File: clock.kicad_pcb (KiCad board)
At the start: 2 copper layers, 129 parts, among them J1 USB_C_Receptacle_USB2.0_16P, J3 Conn_01x02_Pin, J4 Conn_01x02_Pin, Q1 2N7002K, Q2 NPN, U1 STM32F072CBT6, U2 USBLC6-2SC6, U4 MCP73871-2CC, U5 AP2112K-3.3, Y1 8MHz

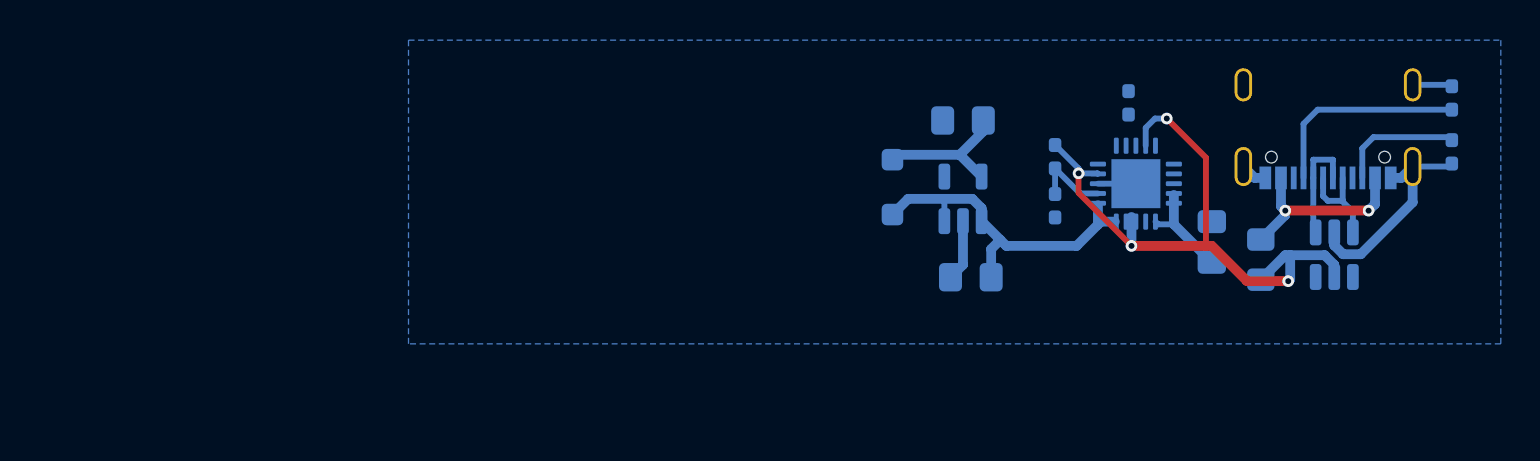
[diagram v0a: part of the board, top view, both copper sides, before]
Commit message: rerouting to flip the usb to the other side
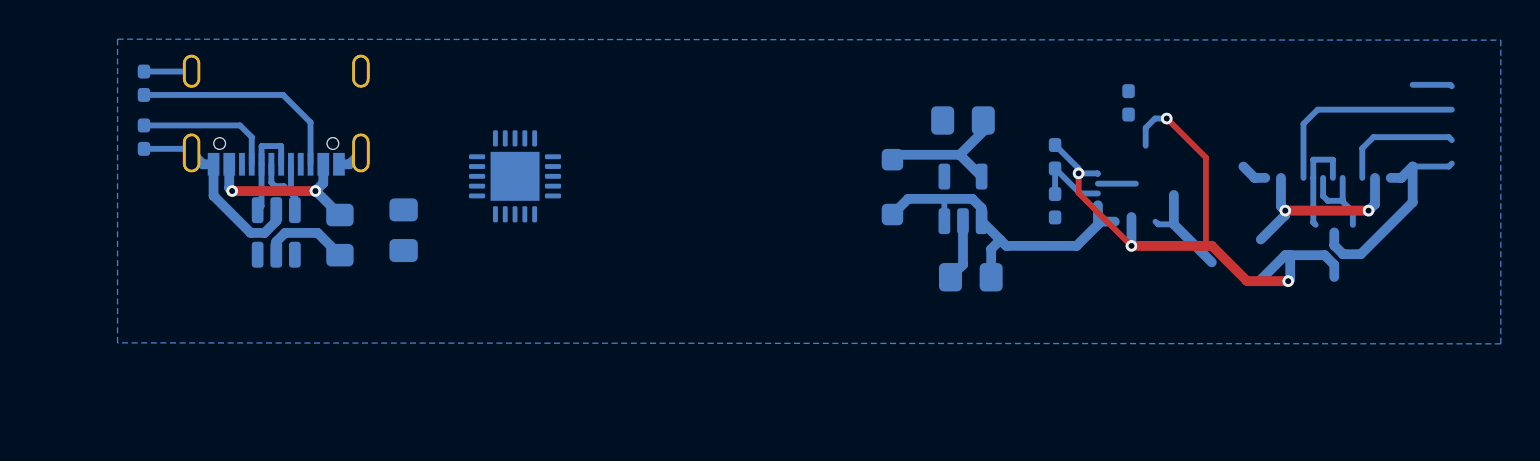
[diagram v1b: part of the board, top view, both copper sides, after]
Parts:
- moved R1 66.8 mm to (206.0, 28.5), turned to -90 degrees
- moved R2 66.8 mm to (206.0, 31.2), turned to 90 degrees
- moved U2 54.0 mm to (212.8, 36.1)
- moved J1 53.7 mm to (212.8, 30.1)
- moved F1 47.0 mm to (216.0, 36.2)
- moved C17 41.3 mm to (219.2, 36.0)
- moved U4 31.7 mm to (224.9, 33.2), turned to 180 degrees
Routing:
- net GND: track 19.7 -> 33.7 mm
- net Net-(J1-CC2): track 6.38 -> 17.6 mm
- net /VBUS: track 9.81 -> 18.8 mm, vias 2 -> 4
- net Net-(J1-CC1): track 10.6 -> 17.8 mm
- net D_BUS-: track 5.30 -> 10.6 mm
- net D_BUS+: track 4.63 -> 9.49 mm
- net +5V: track 34.1 -> 38.7 mm

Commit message: more routing
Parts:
- moved R6 38.7 mm to (218.0, 35.3), turned to -90 degrees
- moved R10 31.4 mm to (221.5, 37.5), turned to 0 degrees
- moved R11 28.6 mm to (224.0, 37.5), turned to 180 degrees
- moved C18 20.7 mm to (227.5, 37.2), turned to 0 degrees
- moved U5 20.3 mm to (227.5, 34.2), turned to 0 degrees
- moved C19 17.4 mm to (231.0, 34.8), turned to -90 degrees
- moved D76 16.2 mm to (228.2, 31.0), turned to 0 degrees
- moved C17 7.56 mm to (223.5, 29.8), turned to 180 degrees
- moved U4 3.52 mm to (221.5, 34.0), turned to 90 degrees
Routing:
- net GND: track 33.7 -> 17.2 mm
- net +5V: track 38.7 -> 26.2 mm
- net Net-(J1-CC1): track 17.8 -> 7.13 mm
- net /VBUS: track 18.8 -> 8.97 mm, vias 4 -> 2
- net Net-(J1-CC2): track 17.6 -> 11.2 mm
- net D_BUS-: track 10.6 -> 5.28 mm
- net Net-(J5-Pin_1): track 5.23 -> 0.00 mm
- net D_BUS+: track 9.49 -> 4.86 mm
- net Net-(U4-VPCC): track 4.02 -> 1.31 mm

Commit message: more routing
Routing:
- net +3.3V: track 7.36 -> 25.0 mm, vias 0 -> 2
- net VCC: track 17.8 -> 14.4 mm
- net GND: track 17.2 -> 14.1 mm
- net LBO: track 0.00 -> 1.87 mm
- net Net-(U4-VPCC): track 1.31 -> 2.92 mm

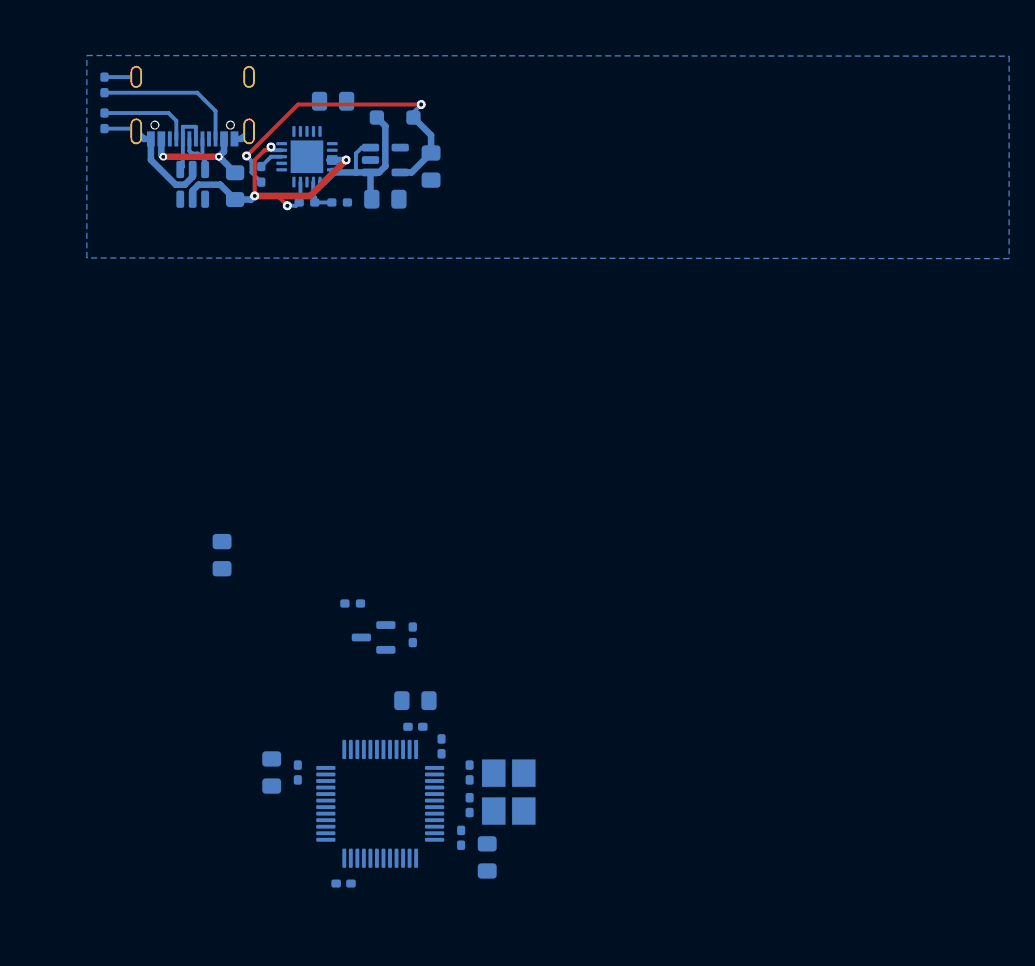
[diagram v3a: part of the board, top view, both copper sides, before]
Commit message: flipped routing now has ground plane
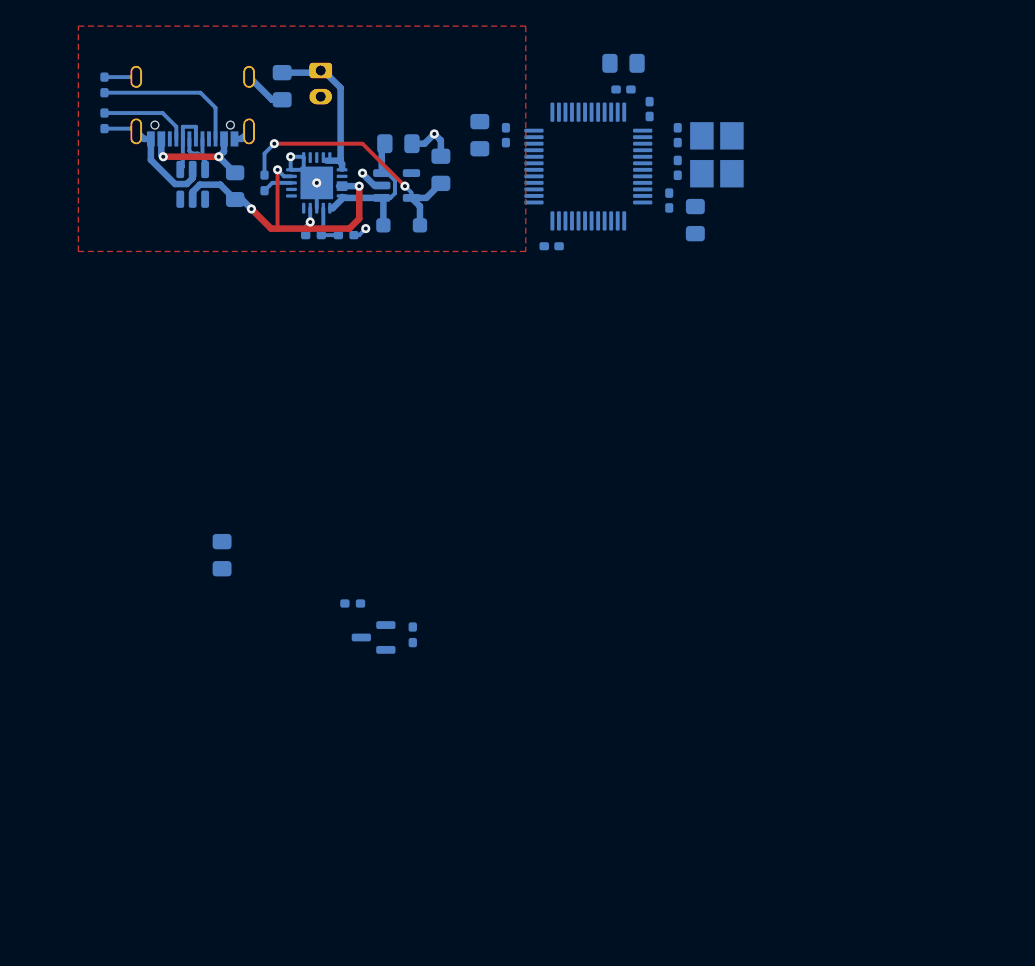
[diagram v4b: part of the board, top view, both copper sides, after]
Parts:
- added J5: Battery, Connector_JST:JST_PH_S2B-PH-K_1x02_P2.00mm_Horizontal, B.Cu at (222.6, 27.4)
- moved C11 51.3 mm to (249.9, 32.4)
- moved C12 51.3 mm to (249.9, 34.9)
- moved Y1 51.3 mm to (252.9, 33.9)
- moved U1 51.3 mm to (243.0, 34.8)
- moved C1 51.3 mm to (245.7, 26.9)
- moved C2 51.3 mm to (247.7, 30.4)
- moved C3 51.3 mm to (245.7, 28.9)
- moved C4 51.3 mm to (240.2, 40.9)
- moved C5 51.3 mm to (234.7, 32.4)
- moved C6 51.3 mm to (236.7, 32.4)
- moved C7 51.3 mm to (251.2, 38.9)
- moved C8 51.3 mm to (249.2, 37.4)
- moved D76 8.27 mm to (228.8, 39.2)
- moved C18 4.37 mm to (228.5, 33.0)
- moved C17 4.07 mm to (219.6, 28.6), turned to -90 degrees
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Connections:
- net Net-(J5-Pin_1) renamed /BAT
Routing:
- net GND: track 14.1 -> 31.6 mm, vias 0 -> 5
- net /BAT: track 0.00 -> 12.4 mm
- net +3.3V: track 25.0 -> 20.2 mm
- net VCC: track 14.4 -> 12.2 mm
- net +5V: track 26.2 -> 28.0 mm
- net Net-(U4-VPCC): track 2.92 -> 3.43 mm
- added copper zone on F.Cu, net GND
- removed copper zone on B.Cu, net GND

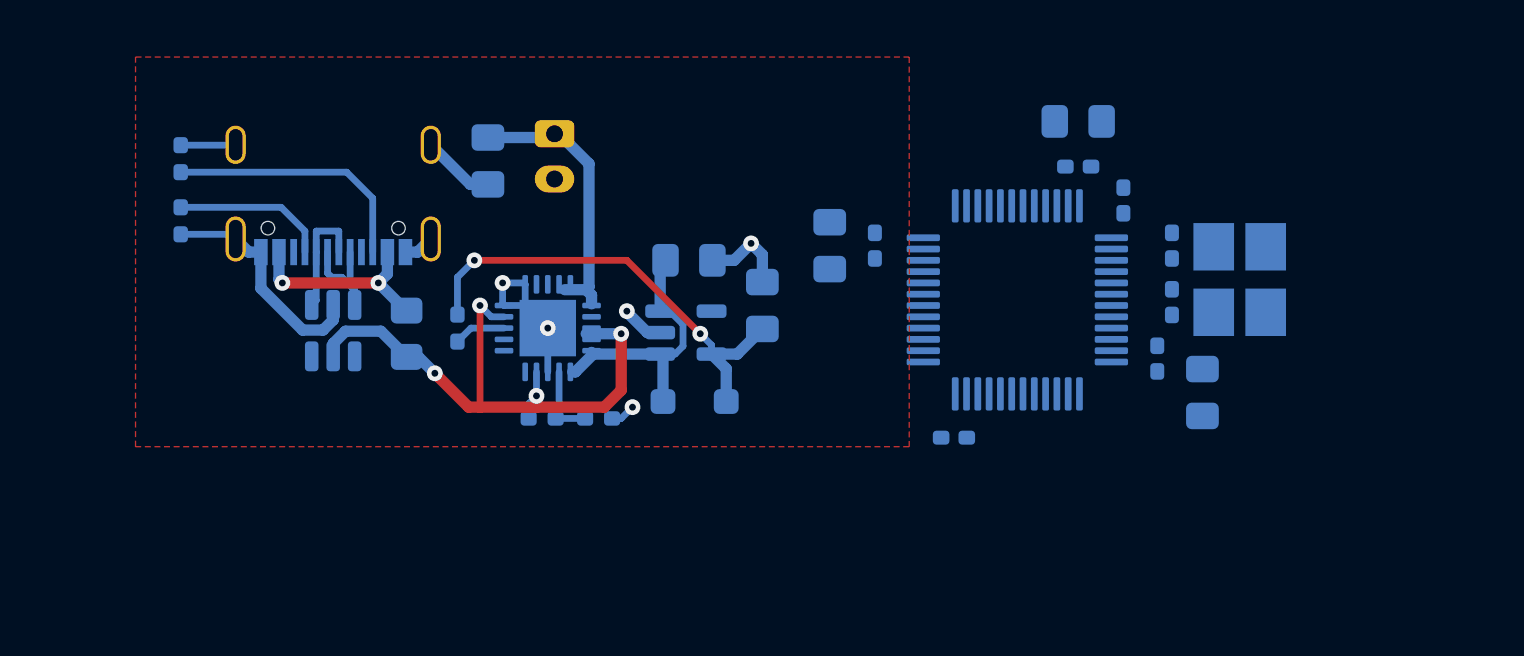
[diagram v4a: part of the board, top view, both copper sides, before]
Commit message: more routing, diff pair, 3V3 to chip etc.
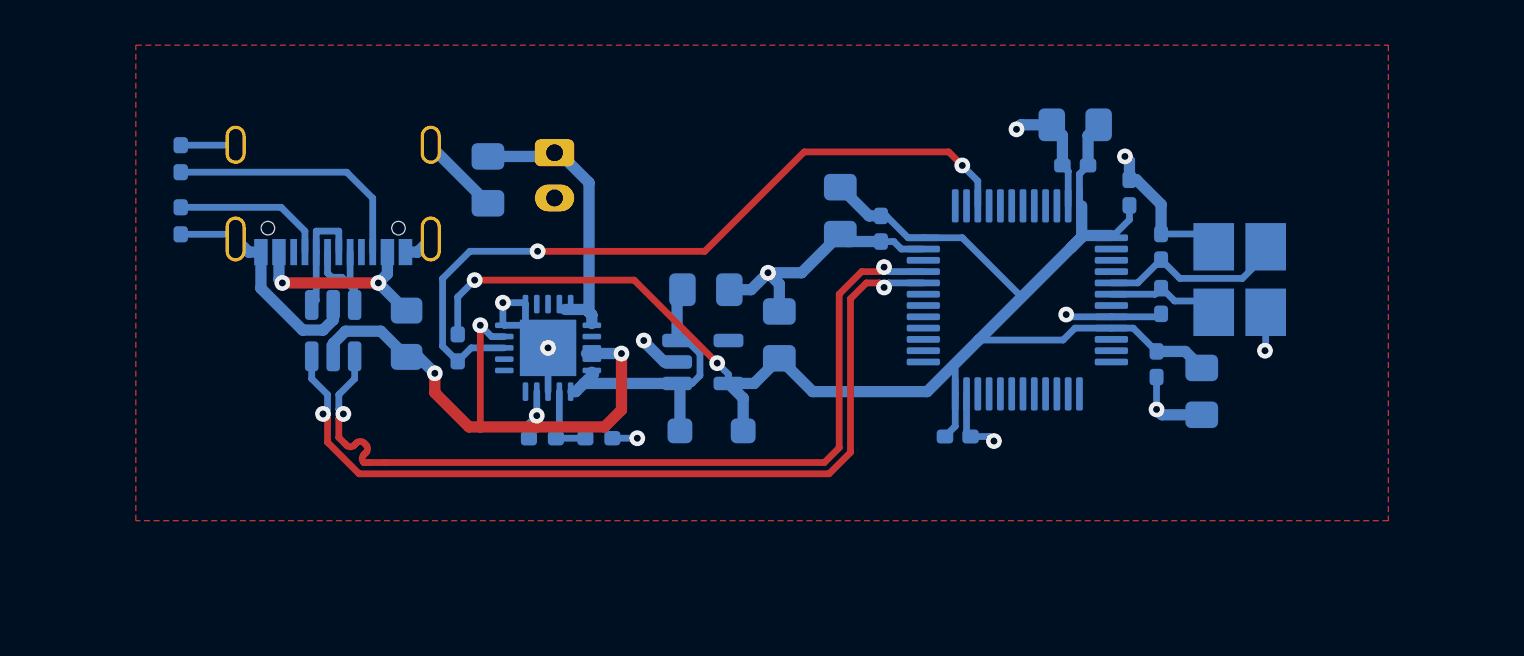
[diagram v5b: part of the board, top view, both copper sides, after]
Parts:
- moved C5 1.62 mm to (235.2, 30.8)
- moved C18 1.50 mm to (229.2, 34.3)
- moved C19 1.50 mm to (232.5, 36.3)
- moved D76 1.50 mm to (229.5, 40.5)
- moved U5 1.50 mm to (229.1, 37.5)
- moved R10 0.88 mm to (222.0, 40.9)
- moved R11 0.88 mm to (224.5, 40.9)
- moved R6 0.88 mm to (218.3, 36.9)
- moved U4 0.88 mm to (222.3, 36.9)
- moved J5 0.84 mm to (222.6, 28.2)
- moved C17 0.84 mm to (219.6, 29.4)
- moved C6 0.80 mm to (237.0, 31.6)
- moved C12 0.48 mm to (249.4, 34.8)
- moved C11 0.48 mm to (249.4, 32.4)
- moved C2 0.44 mm to (248.0, 30.0)
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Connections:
- U1 pad 39: unconnected-(U1-PB3-Pad39) -> LBO
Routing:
- net +3.3V: track 20.2 -> 75.5 mm
- net D-: track 0.00 -> 38.9 mm, vias 0 -> 2
- net D+: track 0.00 -> 38.8 mm, vias 0 -> 2
- net GND: track 31.6 -> 64.8 mm, vias 5 -> 11
- net LBO: track 2.31 -> 33.9 mm, vias 0 -> 2
- net OSC_IN: track 0.00 -> 8.40 mm
- net OSC_OUT: track 0.00 -> 5.08 mm
- net VCC: track 12.2 -> 13.3 mm
- net +5V: track 28.0 -> 28.7 mm

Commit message: routing
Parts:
- moved C13 86.4 mm to (241.8, 27.8), turned to 90 degrees
- moved R4 84.3 mm to (239.5, 27.8), turned to 90 degrees
- moved BOOT 81.2 mm to (236.8, 28.0), turned to -90 degrees
- moved J3 74.0 mm to (253.5, 28.0), turned to -90 degrees
- moved C5 1.73 mm to (235.5, 32.5)
- moved J5 0.36 mm to (222.3, 28.5)
- moved C17 0.36 mm to (219.2, 29.5)
- moved C6 0.29 mm to (237.2, 31.8)
- moved C1 0.25 mm to (245.6, 27.2)
- renumbered J4 to BOOT
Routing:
- net NRST: track 0.00 -> 13.1 mm, vias 0 -> 2
- net BOOT: track 0.00 -> 8.58 mm
- net GND: track 64.8 -> 70.3 mm
- net +3.3V: track 75.5 -> 78.5 mm
